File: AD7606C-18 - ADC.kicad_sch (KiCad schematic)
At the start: 9 parts, among them IC1 AD7606C-18BSTZ

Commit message: Rename the project to OPEN_PHASE
PhaseSense-8586 was named after the first parts of the design (INA240 +
ADS8586S), which are no longer on the board. OPEN_PHASE follows
OPEN_WEIGHT, the other OPEN THRUST LAB board.

- project files: OPEN_PHASE.kicad_pro / _sch / _pcb / _prl / _dru
- libraries: lib/lib_sym/OPEN_PHASE.kicad_sym and
  lib/lib_fp/OPEN_PHASE.pretty, nickname OPEN_PHASE in both tables, in
  every lib_id and in every footprint of the PCB
- project name of every symbol and sheet instance, so the reference
  designators are kept
- PROJECT_NAME and GIT_URL in the project and in kibot_main.yaml, README
  and its template, CHANGELOG, LTspice headers and their generator
- the README note now says the project was first published as
  PhaseSense-8586

The GitHub repository is now foukouda/OPEN_PHASE. The board name
PHASETRACKER is unchanged. The netlist, ERC and DRC reports are the same
before and after the rename.

Co-Authored-By: Claude Opus 5.5 <noreply@anthropic.com>
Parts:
- C20, C21, C35, C36, C37, C38, C41: footprint PhaseSense-8586:C_0603_1608Metric -> OPEN_PHASE:C_0603_1608Metric; symbol PhaseSense-8586:C -> OPEN_PHASE:C
- C39: footprint PhaseSense-8586:C_0805_2012Metric -> OPEN_PHASE:C_0805_2012Metric; symbol PhaseSense-8586:C_4T -> OPEN_PHASE:C_4T
- IC1: footprint PhaseSense-8586:QFP50P1200X1200X160-64N -> OPEN_PHASE:QFP50P1200X1200X160-64N; symbol PhaseSense-8586:AD7606C-18BSTZ -> OPEN_PHASE:AD7606C-18BSTZ
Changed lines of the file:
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@@
 	)
 	(symbol
-		(lib_id "PhaseSense-8586:C")
+		(lib_id "OPEN_PHASE:C")
 		(at 223.52 95.25 180)
 		(unit 1)
@@
 			)
 		)
-		(property "Footprint" "PhaseSense-8586:C_0603_1608Metric"
+		(property "Footprint" "OPEN_PHASE:C_0603_1608Metric"
 			(at 222.5548 91.44 0)
 			(hide yes)
@@
 		)
 		(instances
-			(project "PhaseSense-8586"
+			(project "OPEN_PHASE"
 				(path "/f9e05184-c88b-4a88-ae9c-ab2bdb32be7c/c5103ceb-5325-4a84-a025-9638a412984e/f06537ee-772d-44d3-8c50-e0ba41038c9c"
 					(reference "C21")
@@
 	)
 	(symbol
-		(lib_id "PhaseSense-8586:C")
+		(lib_id "OPEN_PHASE:C")
 		(at 172.72 45.72 270)
 		(unit 1)
@@
 			)
 		)
-		(property "Footprint" "PhaseSense-8586:C_0603_1608Metric"
+		(property "Footprint" "OPEN_PHASE:C_0603_1608Metric"
 			(at 168.91 46.6852 0)
 			(hide yes)
@@
 		)
 		(instances
-			(project "PhaseSense-8586"
+			(project "OPEN_PHASE"
 				(path "/f9e05184-c88b-4a88-ae9c-ab2bdb32be7c/c5103ceb-5325-4a84-a025-9638a412984e/f06537ee-772d-44d3-8c50-e0ba41038c9c"
 					(reference "C41")
@@
 		)
 		(instances
-			(project "PhaseSense-8586"
+			(project "OPEN_PHASE"
 				(path "/f9e05184-c88b-4a88-ae9c-ab2bdb32be7c/c5103ceb-5325-4a84-a025-9638a412984e/f06537ee-772d-44d3-8c50-e0ba41038c9c"
 					(reference "#PWR05")
@@
 		)
 		(instances
-			(project "PhaseSense-8586"
+			(project "OPEN_PHASE"
 				(path "/f9e05184-c88b-4a88-ae9c-ab2bdb32be7c/c5103ceb-5325-4a84-a025-9638a412984e/f06537ee-772d-44d3-8c50-e0ba41038c9c"
 					(reference "#PWR038")
@@
 		)
 		(instances
-			(project "PhaseSense-8586"
+			(project "OPEN_PHASE"
 				(path "/f9e05184-c88b-4a88-ae9c-ab2bdb32be7c/c5103ceb-5325-4a84-a025-9638a412984e/f06537ee-772d-44d3-8c50-e0ba41038c9c"
 					(reference "#PWR041")
@@
 		)
 		(instances
-			(project "PhaseSense-8586"
+			(project "OPEN_PHASE"
 				(path "/f9e05184-c88b-4a88-ae9c-ab2bdb32be7c/c5103ceb-5325-4a84-a025-9638a412984e/f06537ee-772d-44d3-8c50-e0ba41038c9c"
 					(reference "#PWR040")
@@
 		)
 		(instances
-			(project "PhaseSense-8586"
+			(project "OPEN_PHASE"
 				(path "/f9e05184-c88b-4a88-ae9c-ab2bdb32be7c/c5103ceb-5325-4a84-a025-9638a412984e/f06537ee-772d-44d3-8c50-e0ba41038c9c"
 					(reference "#PWR030")
@@
 		)
 		(instances
-			(project "PhaseSense-8586"
+			(project "OPEN_PHASE"
 				(path "/f9e05184-c88b-4a88-ae9c-ab2bdb32be7c/c5103ceb-5325-4a84-a025-9638a412984e/f06537ee-772d-44d3-8c50-e0ba41038c9c"
 					(reference "#PWR026")
@@
 		)
 		(instances
-			(project "PhaseSense-8586"
+			(project "OPEN_PHASE"
 				(path "/f9e05184-c88b-4a88-ae9c-ab2bdb32be7c/c5103ceb-5325-4a84-a025-9638a412984e/f06537ee-772d-44d3-8c50-e0ba41038c9c"
 					(reference "#PWR037")
@@
 	)
 	(symbol
-		(lib_id "PhaseSense-8586:AD7606C-18BSTZ")
+		(lib_id "OPEN_PHASE:AD7606C-18BSTZ")
 		(at 153.67 114.3 90)
 		(unit 1)
@@
 			)
 		)
-		(property "Footprint" "PhaseSense-8586:QFP50P1200X1200X160-64N"
+		(property "Footprint" "OPEN_PHASE:QFP50P1200X1200X160-64N"
 			(at 238.43 64.77 0)
 			(hide yes)
@@
 		)
 		(instances
-			(project "PhaseSense-8586"
+			(project "OPEN_PHASE"
 				(path "/f9e05184-c88b-4a88-ae9c-ab2bdb32be7c/c5103ceb-5325-4a84-a025-9638a412984e/f06537ee-772d-44d3-8c50-e0ba41038c9c"
 					(reference "IC1")
@@
 		)
 		(instances
-			(project "PhaseSense-8586"
+			(project "OPEN_PHASE"
 				(path "/f9e05184-c88b-4a88-ae9c-ab2bdb32be7c/c5103ceb-5325-4a84-a025-9638a412984e/f06537ee-772d-44d3-8c50-e0ba41038c9c"
 					(reference "#PWR029")
@@
 	)
 	(symbol
-		(lib_id "PhaseSense-8586:C")
+		(lib_id "OPEN_PHASE:C")
 		(at 157.48 124.46 90)
 		(unit 1)
@@
 			)
 		)
-		(property "Footprint" "PhaseSense-8586:C_0603_1608Metric"
+		(property "Footprint" "OPEN_PHASE:C_0603_1608Metric"
 			(at 161.29 123.4948 0)
 			(hide yes)
@@
 		)
 		(instances
-			(project "PhaseSense-8586"
+			(project "OPEN_PHASE"
 				(path "/f9e05184-c88b-4a88-ae9c-ab2bdb32be7c/c5103ceb-5325-4a84-a025-9638a412984e/f06537ee-772d-44d3-8c50-e0ba41038c9c"
 					(reference "C20")
@@
 	)
 	(symbol
-		(lib_id "PhaseSense-8586:C")
+		(lib_id "OPEN_PHASE:C")
 		(at 176.53 55.88 180)
 		(unit 1)
@@
 			)
 		)
-		(property "Footprint" "PhaseSense-8586:C_0603_1608Metric"
+		(property "Footprint" "OPEN_PHASE:C_0603_1608Metric"
 			(at 175.5648 52.07 0)
 			(hide yes)
@@
 		)
 		(instances
-			(project "PhaseSense-8586"
+			(project "OPEN_PHASE"
 				(path "/f9e05184-c88b-4a88-ae9c-ab2bdb32be7c/c5103ceb-5325-4a84-a025-9638a412984e/f06537ee-772d-44d3-8c50-e0ba41038c9c"
 					(reference "C36")
@@
 		)
 		(instances
-			(project "PhaseSense-8586"
+			(project "OPEN_PHASE"
 				(path "/f9e05184-c88b-4a88-ae9c-ab2bdb32be7c/c5103ceb-5325-4a84-a025-9638a412984e/f06537ee-772d-44d3-8c50-e0ba41038c9c"
 					(reference "#PWR048")
@@
 		)
 		(instances
-			(project "PhaseSense-8586"
+			(project "OPEN_PHASE"
 				(path "/f9e05184-c88b-4a88-ae9c-ab2bdb32be7c/c5103ceb-5325-4a84-a025-9638a412984e/f06537ee-772d-44d3-8c50-e0ba41038c9c"
 					(reference "#PWR028")
@@
 	)
 	(symbol
-		(lib_id "PhaseSense-8586:C")
+		(lib_id "OPEN_PHASE:C")
 		(at 154.94 49.53 270)
 		(unit 1)
@@
 			)
 		)
-		(property "Footprint" "PhaseSense-8586:C_0603_1608Metric"
+		(property "Footprint" "OPEN_PHASE:C_0603_1608Metric"
 			(at 151.13 50.4952 0)
 			(hide yes)
@@
 		)
 		(instances
-			(project "PhaseSense-8586"
+			(project "OPEN_PHASE"
 				(path "/f9e05184-c88b-4a88-ae9c-ab2bdb32be7c/c5103ceb-5325-4a84-a025-9638a412984e/f06537ee-772d-44d3-8c50-e0ba41038c9c"
 					(reference "C35")
@@
 		)
 		(instances
-			(project "PhaseSense-8586"
+			(project "OPEN_PHASE"
 				(path "/f9e05184-c88b-4a88-ae9c-ab2bdb32be7c/c5103ceb-5325-4a84-a025-9638a412984e/f06537ee-772d-44d3-8c50-e0ba41038c9c"
 					(reference "#PWR039")
@@
 	)
 	(symbol
-		(lib_id "PhaseSense-8586:C")
+		(lib_id "OPEN_PHASE:C")
 		(at 182.88 55.88 180)
 		(unit 1)
@@
 			)
 		)
-		(property "Footprint" "PhaseSense-8586:C_0603_1608Metric"
+		(property "Footprint" "OPEN_PHASE:C_0603_1608Metric"
 			(at 181.9148 52.07 0)
 			(hide yes)
@@
 		)
 		(instances
-			(project "PhaseSense-8586"
+			(project "OPEN_PHASE"
 				(path "/f9e05184-c88b-4a88-ae9c-ab2bdb32be7c/c5103ceb-5325-4a84-a025-9638a412984e/f06537ee-772d-44d3-8c50-e0ba41038c9c"
 					(reference "C37")
@@
 	)
 	(symbol
-		(lib_id "PhaseSense-8586:C")
+		(lib_id "OPEN_PHASE:C")
 		(at 184.15 46.99 270)
 		(unit 1)
@@
 			)
 		)
-		(property "Footprint" "PhaseSense-8586:C_0603_1608Metric"
+		(property "Footprint" "OPEN_PHASE:C_0603_1608Metric"
 			(at 180.34 47.9552 0)
 			(hide yes)
@@
 		)
 		(instances
-			(project "PhaseSense-8586"
+			(project "OPEN_PHASE"
 				(path "/f9e05184-c88b-4a88-ae9c-ab2bdb32be7c/c5103ceb-5325-4a84-a025-9638a412984e/f06537ee-772d-44d3-8c50-e0ba41038c9c"
 					(reference "C38")
@@
 	)
 	(symbol
-		(lib_id "PhaseSense-8586:C_4T")
+		(lib_id "OPEN_PHASE:C_4T")
 		(at 162.56 53.34 0)
 		(unit 1)
@@
 			)
 		)
-		(property "Footprint" "PhaseSense-8586:C_0805_2012Metric"
+		(property "Footprint" "OPEN_PHASE:C_0805_2012Metric"
 			(at 163.5252 57.15 0)
 			(hide yes)
@@
 		)
 		(instances
-			(project "PhaseSense-8586"
+			(project "OPEN_PHASE"
 				(path "/f9e05184-c88b-4a88-ae9c-ab2bdb32be7c/c5103ceb-5325-4a84-a025-9638a412984e/f06537ee-772d-44d3-8c50-e0ba41038c9c"
 					(reference "C39")

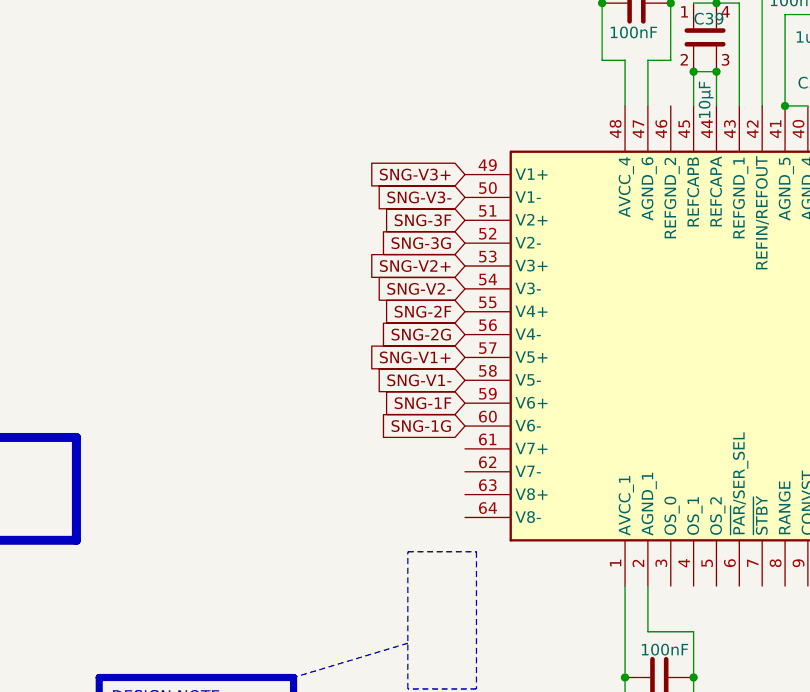
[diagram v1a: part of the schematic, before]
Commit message: Smaller boost inductor, white board, openEMS and thermal simulations
- L1: Wurth 744373965022 (13.5 x 12.5 mm) -> WE-MAPI 4030 74438357022
  (2.2 uH, 4.1 x 4.1 x 3.1 mm, Isat 4.6 A at -10 %, above the 3.1 A LT8362
  switch limit). Footprint and STEP from the KiCad library, copied to lib/.
- Board: solder mask white (custom opaque #F4F4F0F5, the KiCad "White"
  preset renders pink over copper), silkscreen black. kibot_globals.yaml
  names the colours so the fabrication notes print WHITE / BLACK.
- Simulation/openEMS: inductance of the PBV shunts seen by the INA241
  inputs on the routed copper (results.md, figures in Images/Simulation).
- Simulation/Thermal: current density and temperature of the power paths.
- LTspice simulations, figures and README updated; sim07 DC bus figure.
- 3D animation (Images/OPEN_PHASE.mp4, OPEN_PHASE-spin.gif) on the white board.
- XT60PW-F footprint and model, bottom silkscreen cartouches.

Co-Authored-By: Claude Opus 5.5 <noreply@anthropic.com>
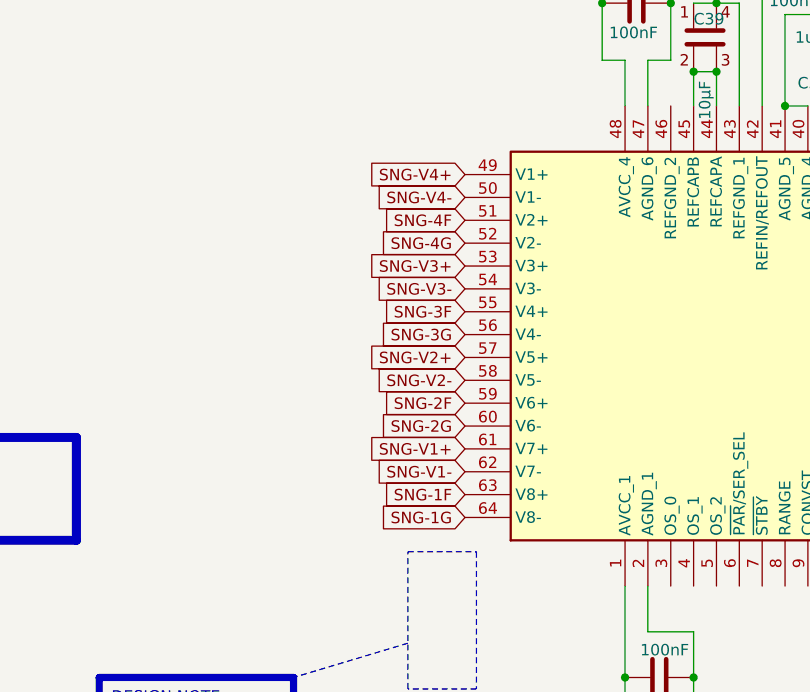
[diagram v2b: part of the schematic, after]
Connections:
- net SNG-1F: now also IC1.63 (V8+); no longer IC1.59 (V6+)
- net SNG-1G: now also IC1.64 (V8-); no longer IC1.60 (V6-)
- net SNG-2F: now also IC1.59 (V6+); no longer IC1.55 (V4+)
- net SNG-2G: now also IC1.60 (V6-); no longer IC1.56 (V4-)
- net SNG-3F: now also IC1.55 (V4+); no longer IC1.51 (V2+)
- net SNG-3G: now also IC1.56 (V4-); no longer IC1.52 (V2-)
- net SNG-V1+: now also IC1.61 (V7+); no longer IC1.57 (V5+)
- net SNG-V1-: now also IC1.62 (V7-); no longer IC1.58 (V5-)
- net SNG-V2+: now also IC1.57 (V5+); no longer IC1.53 (V3+)
- net SNG-V2-: now also IC1.58 (V5-); no longer IC1.54 (V3-)
- net SNG-V3+: now also IC1.53 (V3+); no longer IC1.49 (V1+)
- net SNG-V3-: now also IC1.54 (V3-); no longer IC1.50 (V1-)
- new net SNG-4F: IC1.51 (V2+)
- new net SNG-4G: IC1.52 (V2-)
- new net SNG-V4+: IC1.49 (V1+)
- new net SNG-V4-: IC1.50 (V1-)

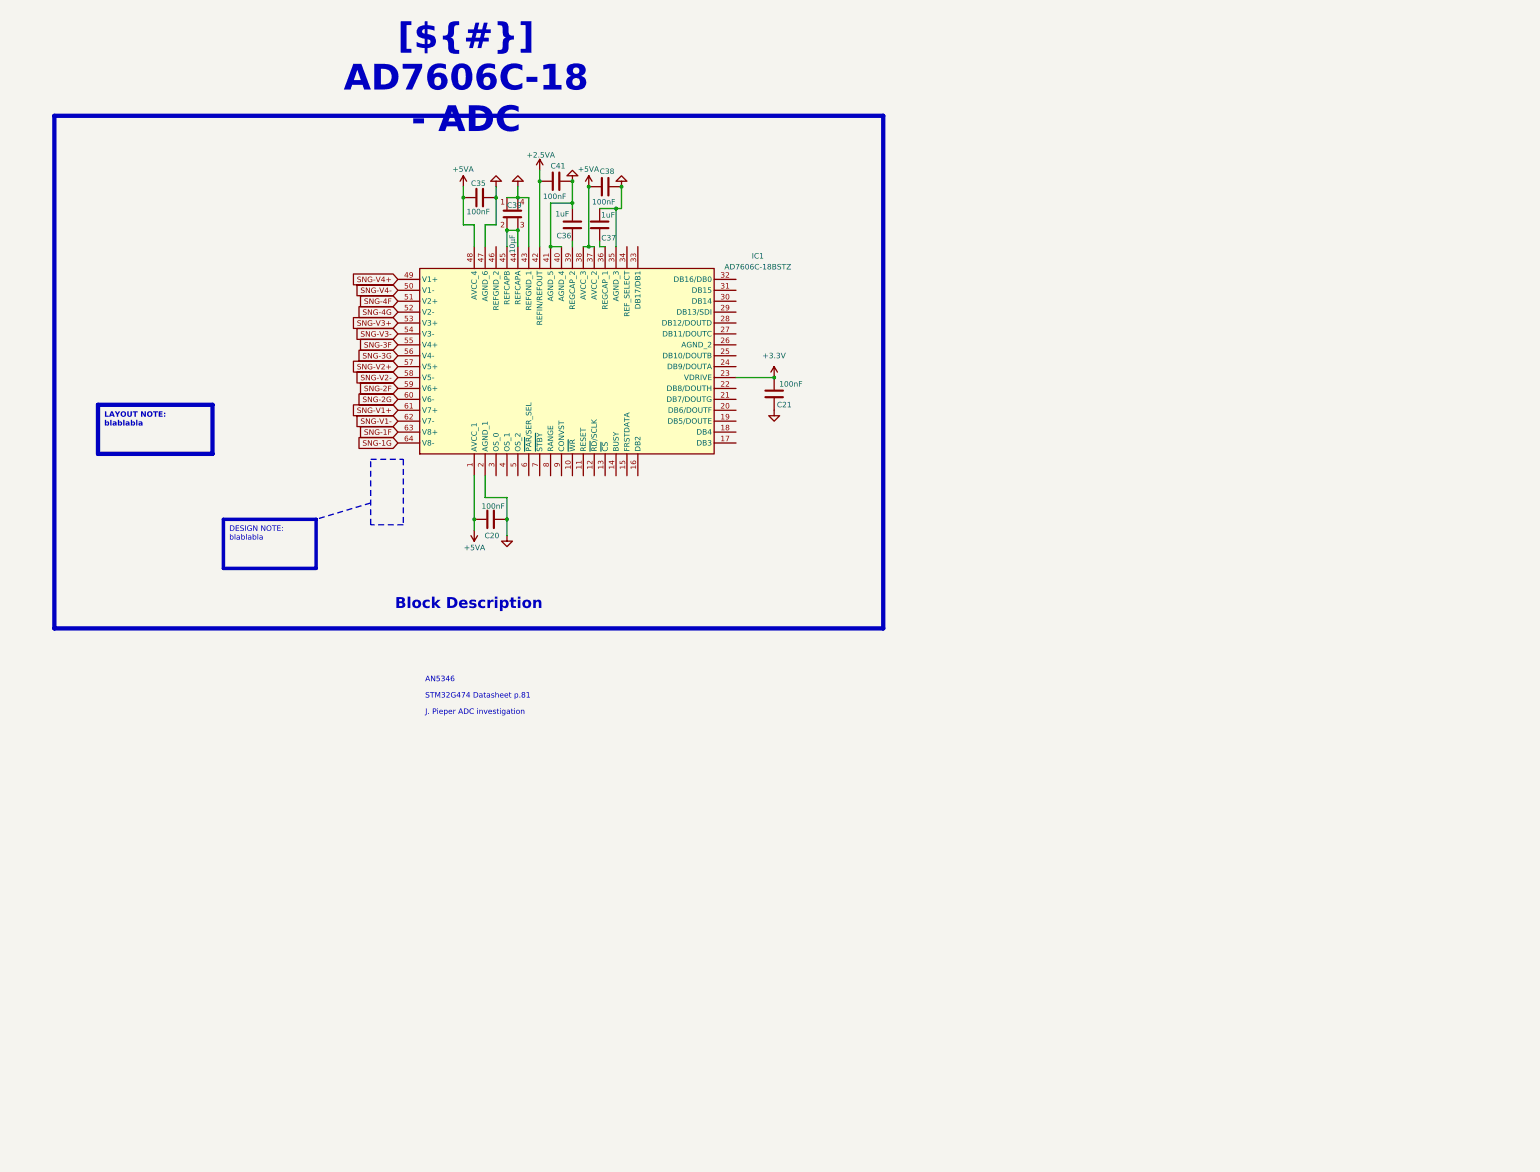
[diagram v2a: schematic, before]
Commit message: Restyle schematic sheets, new title block logo, WE-MAPI inductor in simulations
- Schematic sheets: restyled frames, tables and text boxes
- Title block: INGENIERIE FRANCE logo in KDT_Template_GIT.kicad_wks
- LTspice: L1 modelled as WE-MAPI 4030 74438357022 (22 mOhm),
  simulations 01 and 03 rerun, README and results updated

Co-Authored-By: Claude Opus 5.5 <noreply@anthropic.com>
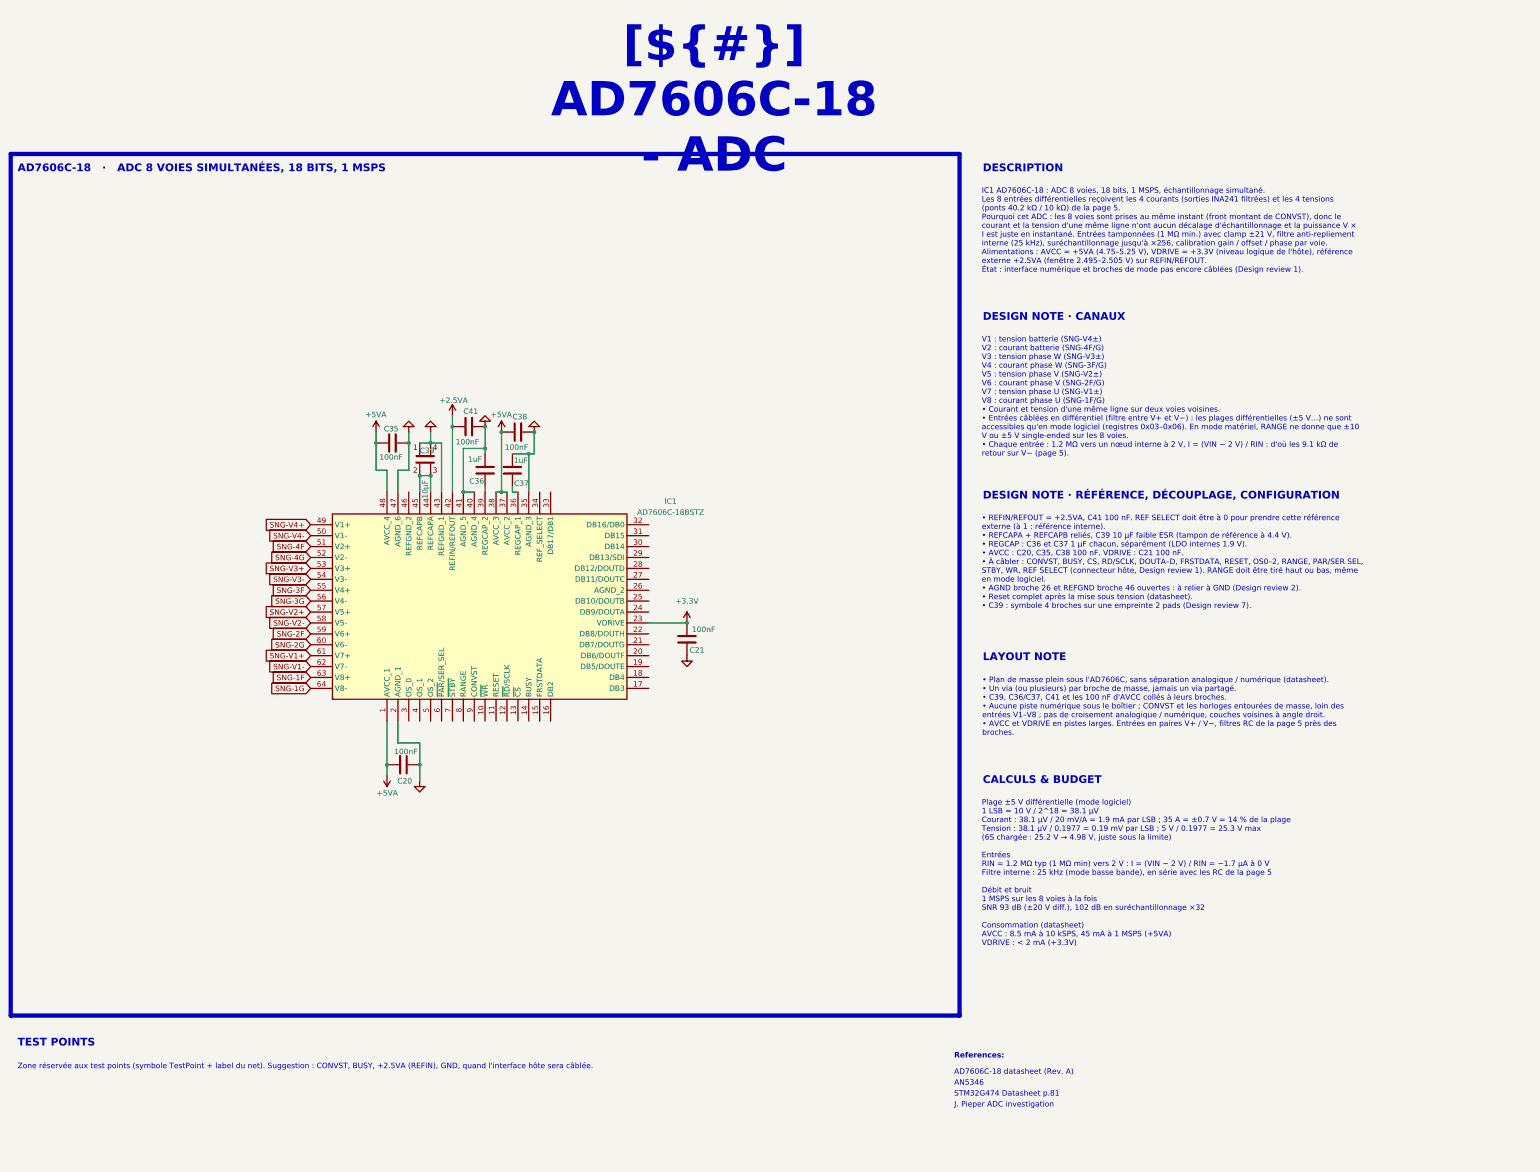
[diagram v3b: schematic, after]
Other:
- note added: "AD7606C-18 datasheet (Rev. A)"
- note added: "References:"
- moved on the sheet: C20, C21, C35, C36, C37, C38, C39, C41, IC1
